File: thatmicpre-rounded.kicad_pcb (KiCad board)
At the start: 2 copper layers, 45 x 24 mm, 12 parts, among them J1 Conn_01x07_Female, U1 THAT1512

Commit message: rounded
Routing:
- net +In: track 31.9 -> 30.2 mm
- net -In: track 23.3 -> 22.2 mm
- net Net-(C1-Pad1): track 12.1 -> 11.1 mm
- net Out: track 52.4 -> 51.4 mm
- net -15V: track 39.3 -> 38.6 mm
- net +15V: track 31.9 -> 31.3 mm

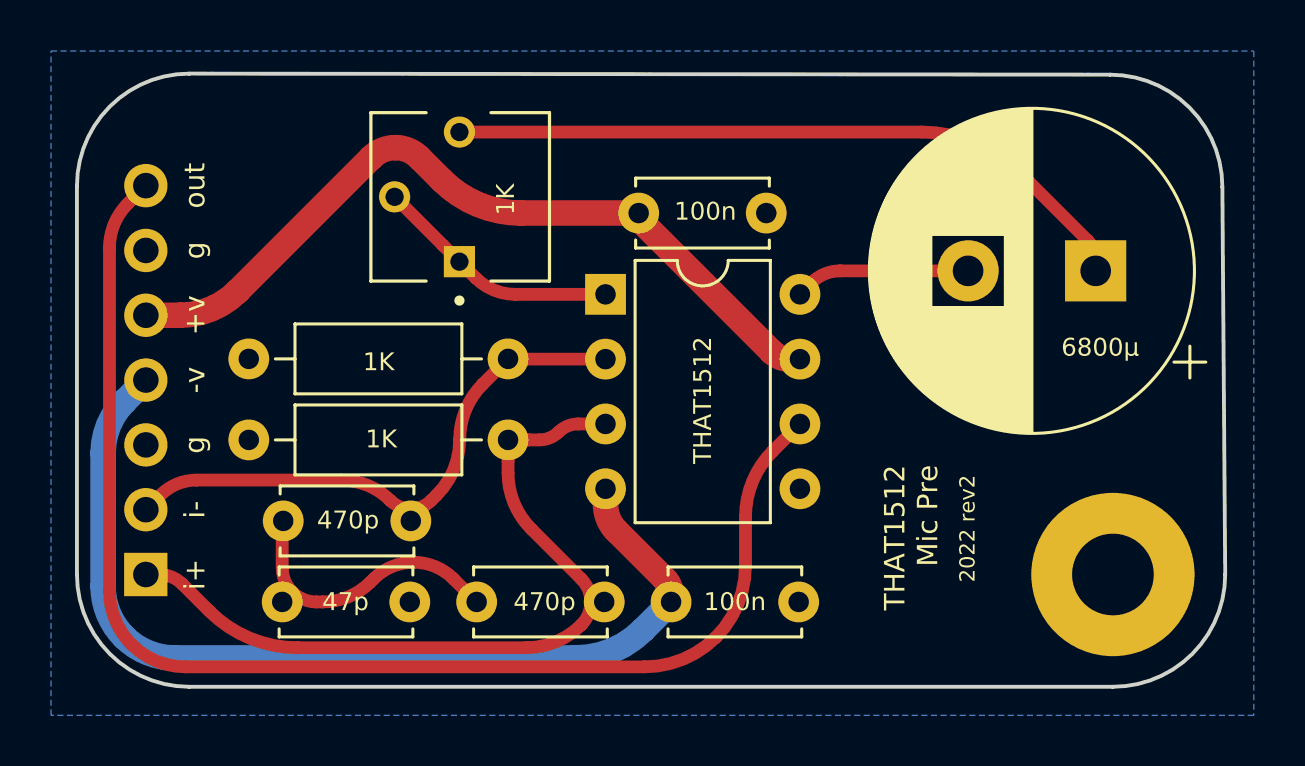
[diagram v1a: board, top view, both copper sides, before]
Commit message: rounded tracks
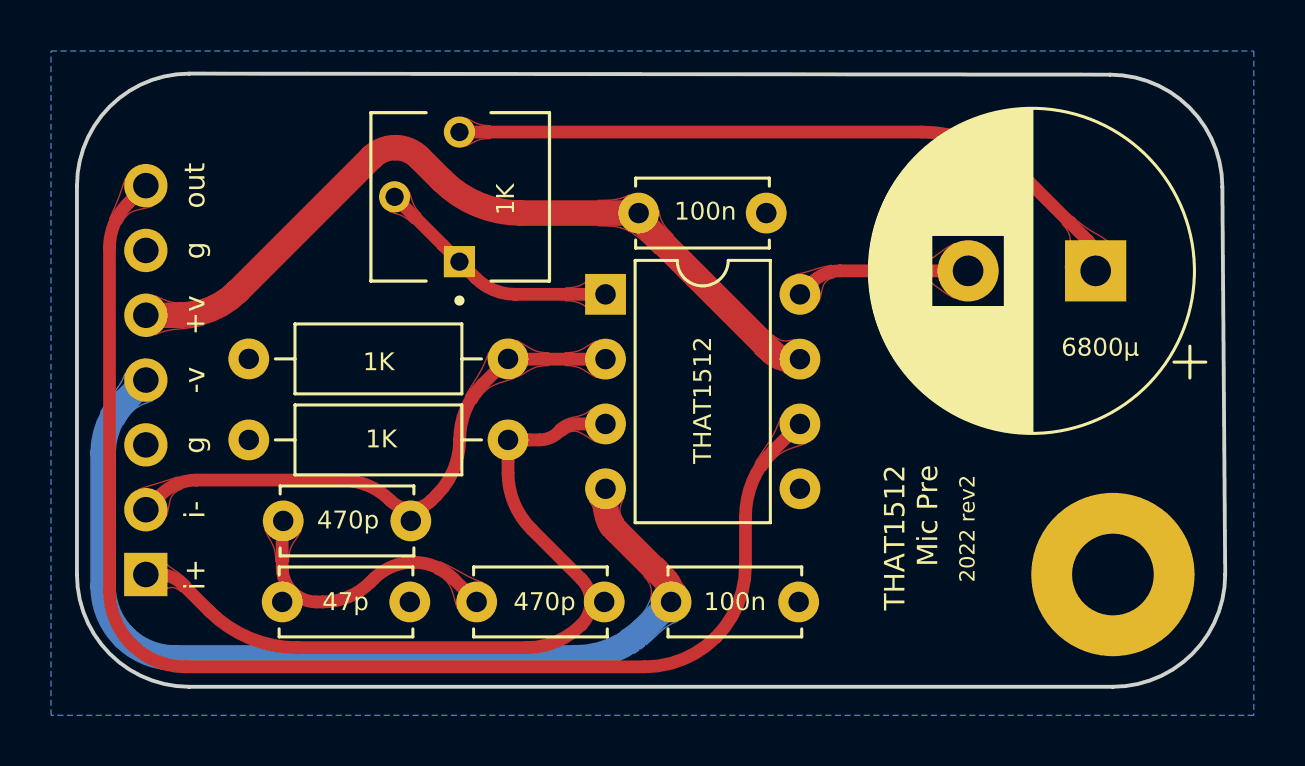
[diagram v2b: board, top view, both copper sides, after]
